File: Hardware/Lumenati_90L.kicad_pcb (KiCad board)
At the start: 2 copper layers, 25.4 x 25.4 mm, 19 parts, among them J1 CONN_041X04_NO_SILK, J2 CONN_041X04_NO_SILK, U1 APA102, U2 APA102, U3 APA102

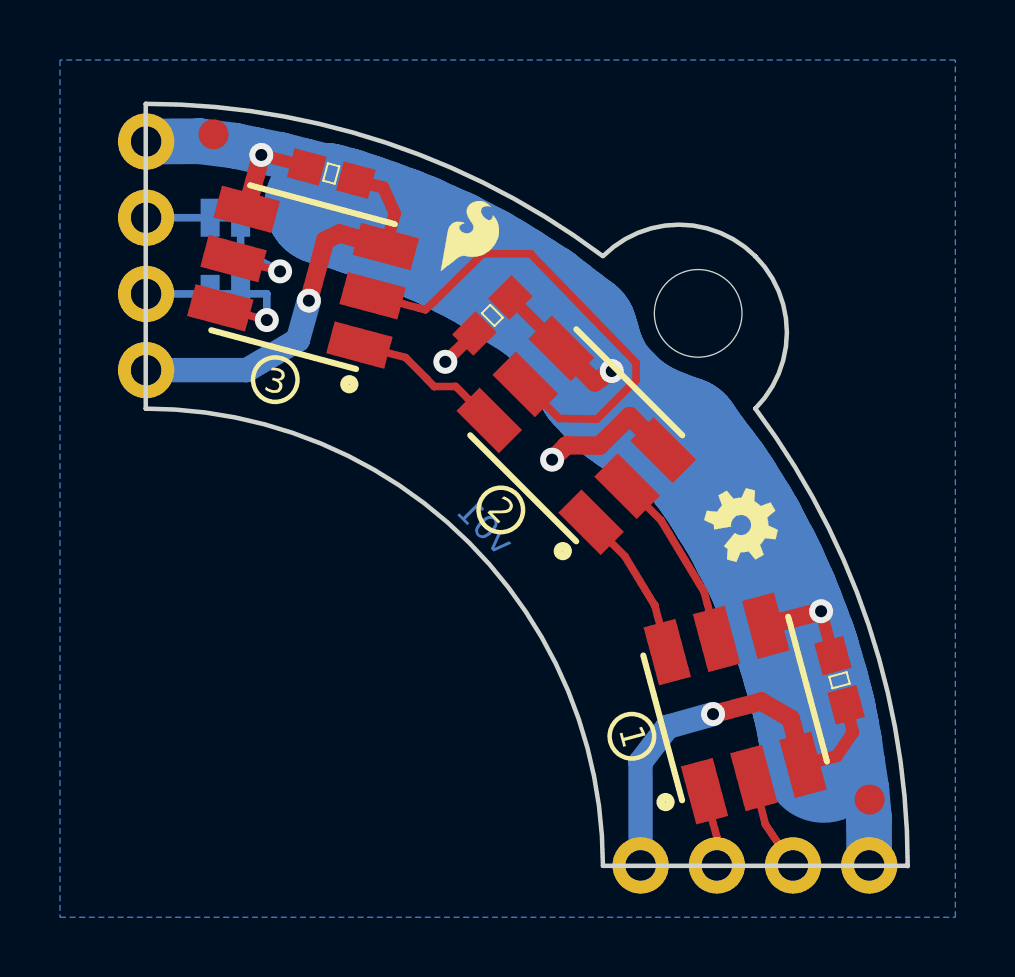
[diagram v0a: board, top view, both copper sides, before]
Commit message: Changed all the names to Lumenati, updated version to v10.
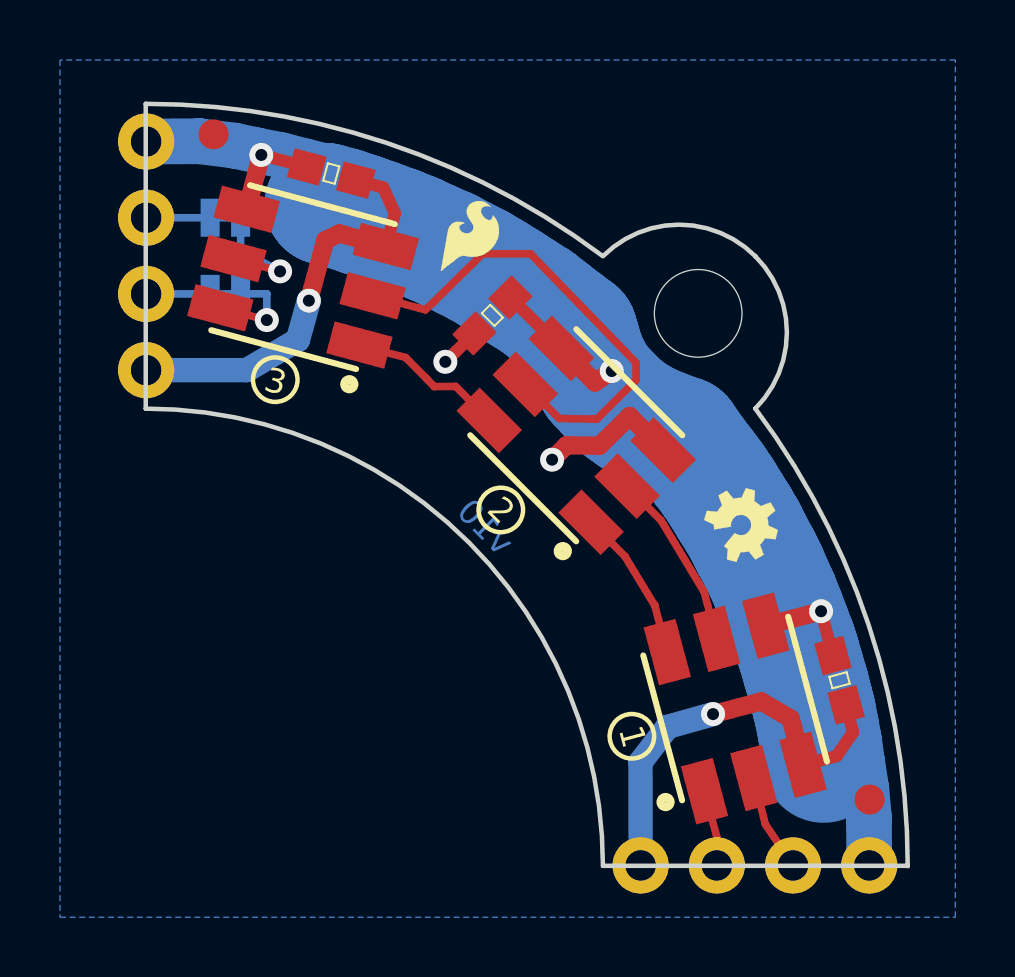
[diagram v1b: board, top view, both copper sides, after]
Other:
- board text added: "Lumenati 90L"
- board text added: "v10"
- board text removed: "HiBeams 90L"
- board text removed: "v01"
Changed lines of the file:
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@@
     (links 24)
     (no_connects 0)
-    (area 124.446872 85.951357 273.2696 194.562)
+    (area 118.770486 85.951357 273.2696 194.562)
     (thickness 1.6)
-    (drawings 32)
+    (drawings 34)
     (tracks 142)
     (zones 0)
@@
       (xy 1.85928 -2.3495) (xy 1.778 -2.4384)) (layer F.SilkS) (width 0.01))
   )
-  (gr_text v01 (at 271.1196 193.167) (layer Cmts.User)
+  (dimension 10.16 (width 0.3) (layer Dwgs.User)
+    (gr_text "0.4000 in" (at 124.4562 94.7928 270) (layer Dwgs.User)
+      (effects (font (size 1.5 1.5) (thickness 0.3)))
+    )
+    (feature1 (pts (xy 131.1148 99.8728) (xy 123.1062 99.8728)))
+    (feature2 (pts (xy 131.1148 89.7128) (xy 123.1062 89.7128)))
+    (crossbar (pts (xy 125.8062 89.7128) (xy 125.8062 99.8728)))
+    (arrow1a (pts (xy 125.8062 99.8728) (xy 125.219779 98.746296)))
+    (arrow1b (pts (xy 125.8062 99.8728) (xy 126.392621 98.746296)))
+    (arrow2a (pts (xy 125.8062 89.7128) (xy 125.219779 90.839304)))
+    (arrow2b (pts (xy 125.8062 89.7128) (xy 126.392621 90.839304)))
+  )
+  (dimension 25.4254 (width 0.3) (layer Dwgs.User)
+    (gr_text "1.0000 in" (at 143.8275 121.2126) (layer Dwgs.User)
+      (effects (font (size 1.5 1.5) (thickness 0.3)))
+    )
+    (feature1 (pts (xy 131.1148 115.1128) (xy 131.1148 122.5626)))
+    (feature2 (pts (xy 156.5402 115.1128) (xy 156.5402 122.5626)))
+    (crossbar (pts (xy 156.5402 119.8626) (xy 131.1148 119.8626)))
+    (arrow1a (pts (xy 131.1148 119.8626) (xy 132.241304 119.276179)))
+    (arrow1b (pts (xy 131.1148 119.8626) (xy 132.241304 120.449021)))
+    (arrow2a (pts (xy 156.5402 119.8626) (xy 155.413696 119.276179)))
+    (arrow2b (pts (xy 156.5402 119.8626) (xy 155.413696 120.449021)))
+  )
+  (gr_text v10 (at 271.1196 193.167) (layer Cmts.User)
     (effects (font (size 1.5 1.5) (thickness 0.3)))
   )
@@
     (effects (font (size 1.5 1.5) (thickness 0.3)))
   )
-  (gr_text "HiBeams 90L" (at 194.3608 189.5348) (layer Cmts.User)
+  (gr_text "Lumenati 90L" (at 194.3608 189.5348) (layer Cmts.User)
     (effects (font (size 1.5 1.5) (thickness 0.3)))
   )
@@
     (effects (font (size 0.8128 0.8128) (thickness 0.1778)))
   )
-  (gr_text v01 (at 142.4432 103.8352 315) (layer B.Cu)
+  (gr_text v10 (at 142.4432 103.8352 315) (layer B.Cu)
     (effects (font (size 0.8128 0.8128) (thickness 0.1778)) (justify mirror))
   )
-  (gr_text "HiBeams 90L" (at 143.9545 102.3239 315) (layer B.SilkS)
+  (gr_text "Lumenati 90L" (at 143.9545 102.3239 315) (layer B.SilkS)
     (effects (font (size 1.5 1.5) (thickness 0.3)) (justify mirror))
   )
